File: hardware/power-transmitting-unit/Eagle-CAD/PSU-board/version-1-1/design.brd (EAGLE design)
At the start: 61 x 35 mm, 65 parts, among them IC1 TPL0401A-10DCKR, IC10 TSC1031, IC2 AP7381-50Y-13, IC3 LT8330, IC4 AP7381-33Y-13, IC5 ADS1115IDGST, IC7 TSC1031, IC8 TSC1031, J2 62201021121

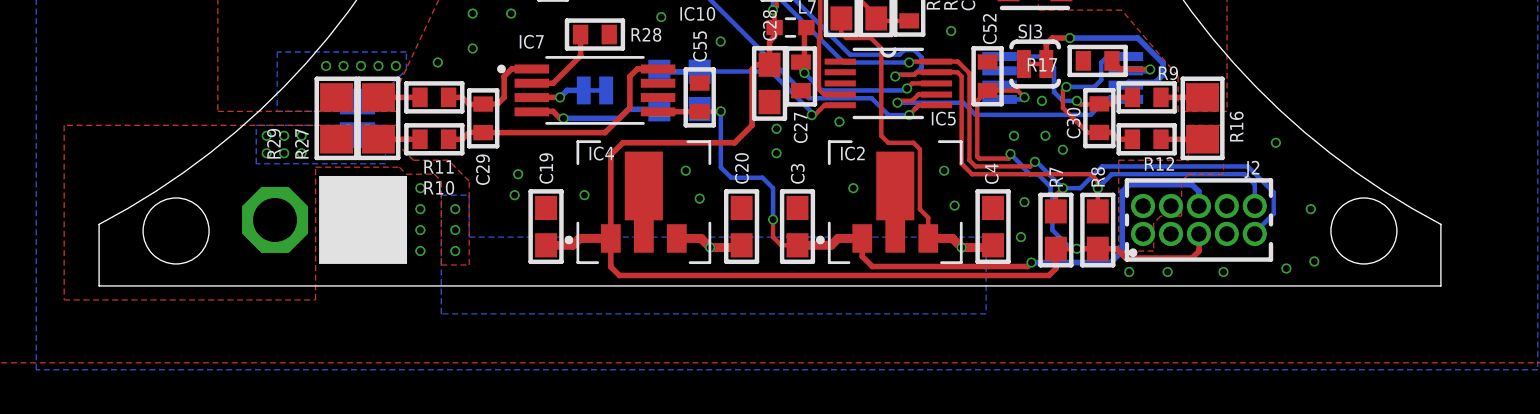
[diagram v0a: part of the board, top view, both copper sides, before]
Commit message: Update firmware and reorganization folders
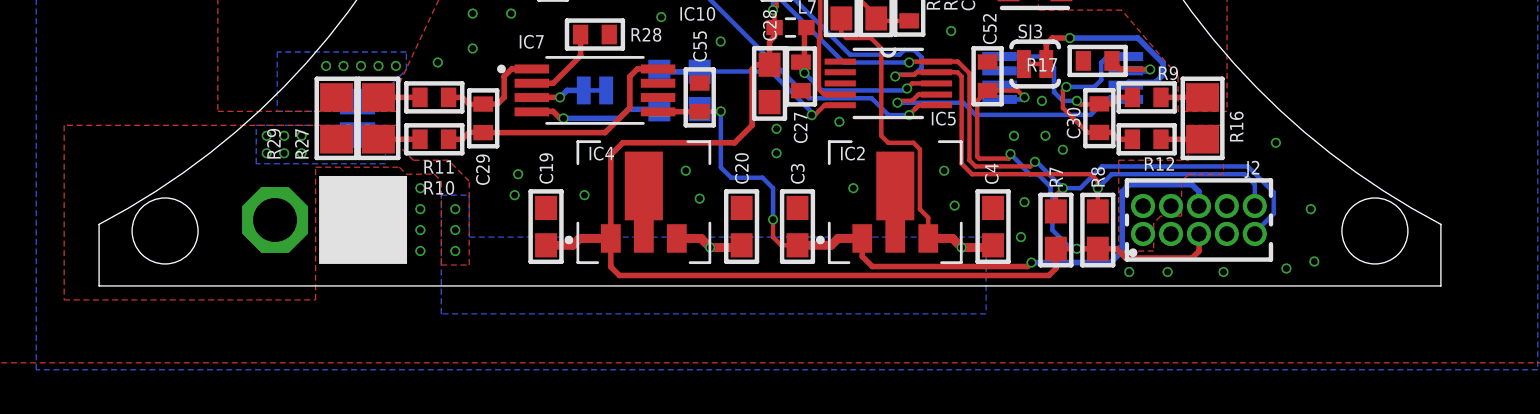
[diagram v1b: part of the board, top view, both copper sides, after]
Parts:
- R18: value 100 -> 100k
- R19: value 100 -> 47k
- R27: value 0.01 -> DNP
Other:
- outline, holes or cut-outs redrawn
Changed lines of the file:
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@@
 <setting verticaltext="up"/>
 </settings>
-<grid distance="6.25" unitdist="mil" unit="mil" style="lines" multiple="1" display="yes" altdistance="5" altunitdist="mil" altunit="mil"/>
+<grid distance="1" unitdist="mm" unit="mm" style="lines" multiple="1" display="yes" altdistance="5" altunitdist="mil" altunit="mil"/>
 <layers>
 <layer number="1" name="Top" color="4" fill="1" visible="yes" active="yes"/>
@@
 <wire x1="17.9" y1="35" x2="0" y2="2.8" width="0" layer="20" curve="-66.549392"/>
 <wire x1="43.1" y1="35" x2="61" y2="2.8" width="0" layer="20" curve="66.549392"/>
-<circle x="3.5" y="2.5" radius="1.5" width="0.01" layer="20"/>
-<circle x="57.5" y="2.5" radius="1.5" width="0.01" layer="20"/>
+<circle x="3" y="2.5" radius="1.5" width="0.01" layer="20"/>
+<circle x="58" y="2.5" radius="1.5" width="0.01" layer="20"/>
 <circle x="21" y="32" radius="1.5" width="0.01" layer="20"/>
 <circle x="40" y="32" radius="1.5" width="0.01" layer="20"/>
@@
 <attribute name="VALUE" x="43.617" y="10.992" size="0.4064" layer="27" font="vector" ratio="10" rot="R180"/>
 </element>
-<element name="R18" library="microbuilder" package="0603" value="100" x="25.47" y="8.8825" smashed="yes" rot="MR270">
+<element name="R18" library="microbuilder" package="0603" value="100k" x="25.47" y="8.8825" smashed="yes" rot="MR270">
 <attribute name="NAME" x="25.0825" y="10.795" size="0.6096" layer="26" font="vector" ratio="10" rot="MR90"/>
 <attribute name="VALUE" x="26.232" y="7.1045" size="0.4064" layer="28" font="vector" ratio="10" rot="MR270"/>
 </element>
-<element name="R19" library="microbuilder" package="0603" value="100" x="27.305" y="8.89" smashed="yes" rot="MR90">
+<element name="R19" library="microbuilder" package="0603" value="47k" x="27.305" y="8.89" smashed="yes" rot="MR90">
 <attribute name="NAME" x="26.9875" y="10.795" size="0.6096" layer="26" font="vector" ratio="10" rot="MR90"/>
 <attribute name="VALUE" x="26.543" y="10.668" size="0.4064" layer="28" font="vector" ratio="10" rot="MR90"/>
 </element>
-<element name="R27" library="microbuilder" package="0805" value="0.01" x="12.7" y="7.62" smashed="yes" rot="R90">
+<element name="R27" library="microbuilder" package="0805" value="DNP" x="12.7" y="7.62" smashed="yes" rot="R90">
 <attribute name="NAME" x="9.525" y="5.715" size="0.6096" layer="25" font="vector" ratio="10" rot="R90"/>
 <attribute name="VALUE" x="13.462" y="9.652" size="0.4064" layer="27" ratio="10" rot="R90"/>
